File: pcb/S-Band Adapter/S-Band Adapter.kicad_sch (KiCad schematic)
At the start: 5 parts, among them J1 CT3151SP-2, J2 FTSH-107-01-L-DV-K-A, J3 ERF8-030-05.0-L-DV-TR, J4 532611071

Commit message: Finished PCB
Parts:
- added J5: CT3151SP-2, KiCad:CT3151SP2, symbol CT3151SP-2:CT3151SP-2
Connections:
- net CAN_A_N: now also J3.03 (CAN_N)
- net CAN_A_P: now also J3.01 (CAN_P)
- net GND: now also J1.1, J1.2, J1.3, J1.4, J2.05 (GND), J2.07 (GND), J2.11 (GND), J3.05 (GND), J3.06 (GND), J3.07 (GND), J3.09 (GND), J3.11 (GND), J3.12 (GND), J3.16 (GND), J3.41 (GND), J3.42 (GND), J3.43 (GND), J3.44 (GND), J3.45 (GND), J3.46 (GND), J3.47 (GND), J3.48 (GND), J3.49 (GND), J3.50 (GND), J3.51 (GND), J3.52 (GND), J3.53 (GND), J3.54 (GND), J3.55 (GND), J3.56 (GND), J3.57 (GND), J3.58 (GND), J4.2 (GND), J4.4 (GND), J4.6 (GND), J4.S1 (SHIELD1), J4.S2 (SHIELD2)
- net VBUS: now also J3.33 (BATPOS), J3.34 (BATPOS), J3.35 (BATPOS), J3.36 (BATPOS), J3.37 (BATPOS), J3.38 (BATPOS), J3.39 (BATPOS), J3.40 (BATPOS), J5.1, J5.2, J5.3, J5.4
- net +3.3V: now reaches J2.03 (3V3)
- net +3.3V: now also J4.10 (3.3V_ref)
- net JTAG_TMS: now reaches J2.04 (JTAG_SWDIO)
- net JTAG_TMS: now also J4.3 (JTMS)
- net JTAG_CLK: now reaches J2.06 (JTAG_SWCLK)
- net JTAG_CLK: now also J2.09 (JTAG_SWCLK), J4.1 (Clock)
- net JTAG_DO: now reaches J2.08 (JTAG_TDO)
- net JTAG_DO: now also J4.5 (JTDO)
- net JTAG_DI: now reaches J2.10 (JTAG_TDI)
- net JTAG_DI: now also J4.7 (JTDI)
- net JTAG_NRST: now reaches J2.12 (JTAG_NRST)
- net JTAG_NRST: now also J4.8 (NRST)
- net UART_P: now reaches J2.13 (STL_MCU_UART)
- net UART_P: now also H101.15 (H1_15)
- net UART_N: now reaches J2.14 (MCU_STL_UART)
- net UART_N: now also H101.13 (H1_13)
- no-connect marks 92 -> 120
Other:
- note added: "Backplane Connector"
- note added: "Banana Plugs"
- note added: "S-Band MCU Connector"
- note added: "S-Band Main Connector"
- note added: "ST-Link Connector"
- moved on the sheet: H101A, H101B, H101C, J1, J2, J3, J4

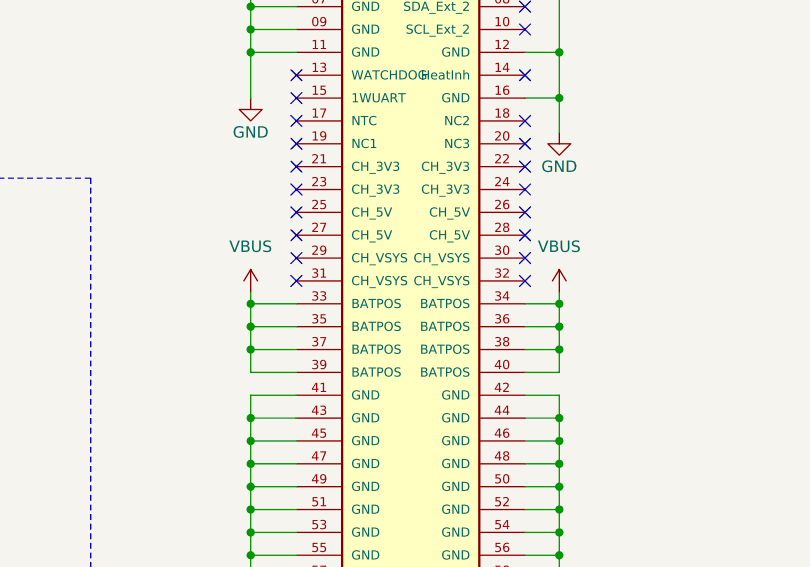
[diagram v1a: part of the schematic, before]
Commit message: Fixed Pulling VSYS from BATPOS
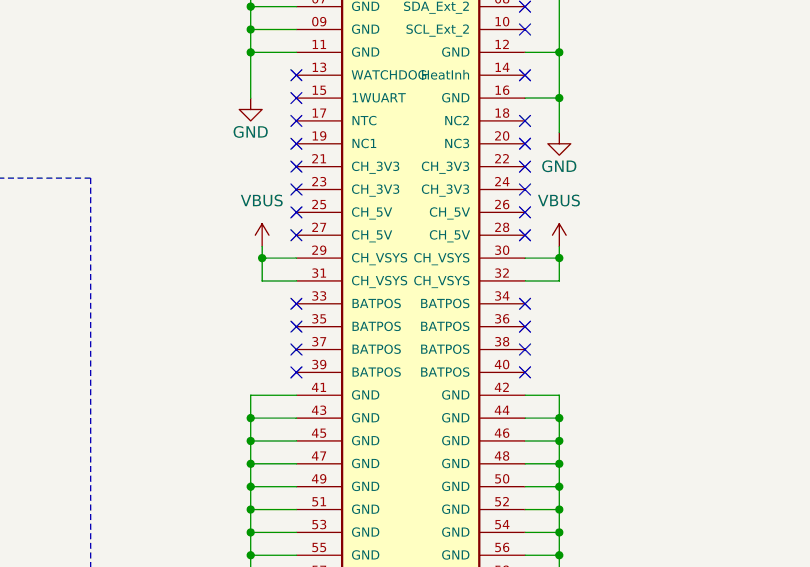
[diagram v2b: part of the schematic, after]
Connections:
- net VBUS: now also J3.29 (CH_VSYS), J3.30 (CH_VSYS), J3.31 (CH_VSYS), J3.32 (CH_VSYS); no longer J3.33 (BATPOS), J3.34 (BATPOS), J3.35 (BATPOS), J3.36 (BATPOS), J3.37 (BATPOS), J3.38 (BATPOS), J3.39 (BATPOS), J3.40 (BATPOS)
- no-connect marks 120 -> 124

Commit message: Added Debug_Reset button & fixed VBAT label
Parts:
- added C1: 100nF, Capacitor_SMD:C_0805_2012Metric_Pad1.18x1.45mm_HandSolder, symbol Device:C_Small
- added S1: 430152050826, 430152050826:430152050826, symbol 430152050826:430152050826
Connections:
- net GND: now also C1.2, S1.2, S1.4
- net DEBUG_Reset: now reaches J4.9 (Debug_reset)
- net DEBUG_Reset: now also C1.1, S1.1, S1.3
- no-connect marks 124 -> 123
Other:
- note added: "Debug Reset"
